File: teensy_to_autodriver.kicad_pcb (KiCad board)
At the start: 2 copper layers, 114.3 x 50.8 mm, 11 parts, among them J1 PIN_ARRAY_5X2, J2 PIN_ARRAY_3X2, J3 PIN_ARRAY_2X1, J4 PIN_ARRAY_2X1, J5 PIN_ARRAY_2X1, J6 PIN_ARRAY_2X1, M0 VAL**, M1 VAL**, M2 VAL**, M3 VAL**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

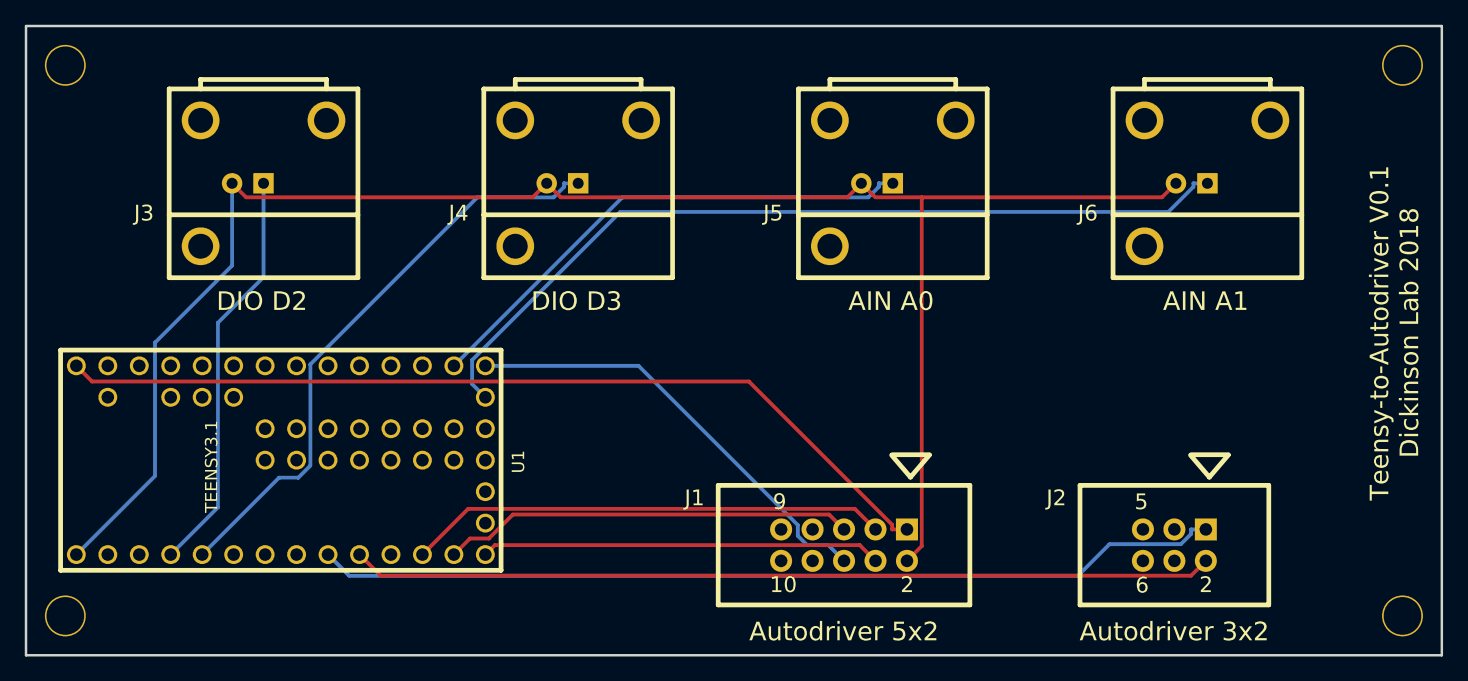
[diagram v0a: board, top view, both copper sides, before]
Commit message: Created version 0.2 of design. Added header for angle sensor.
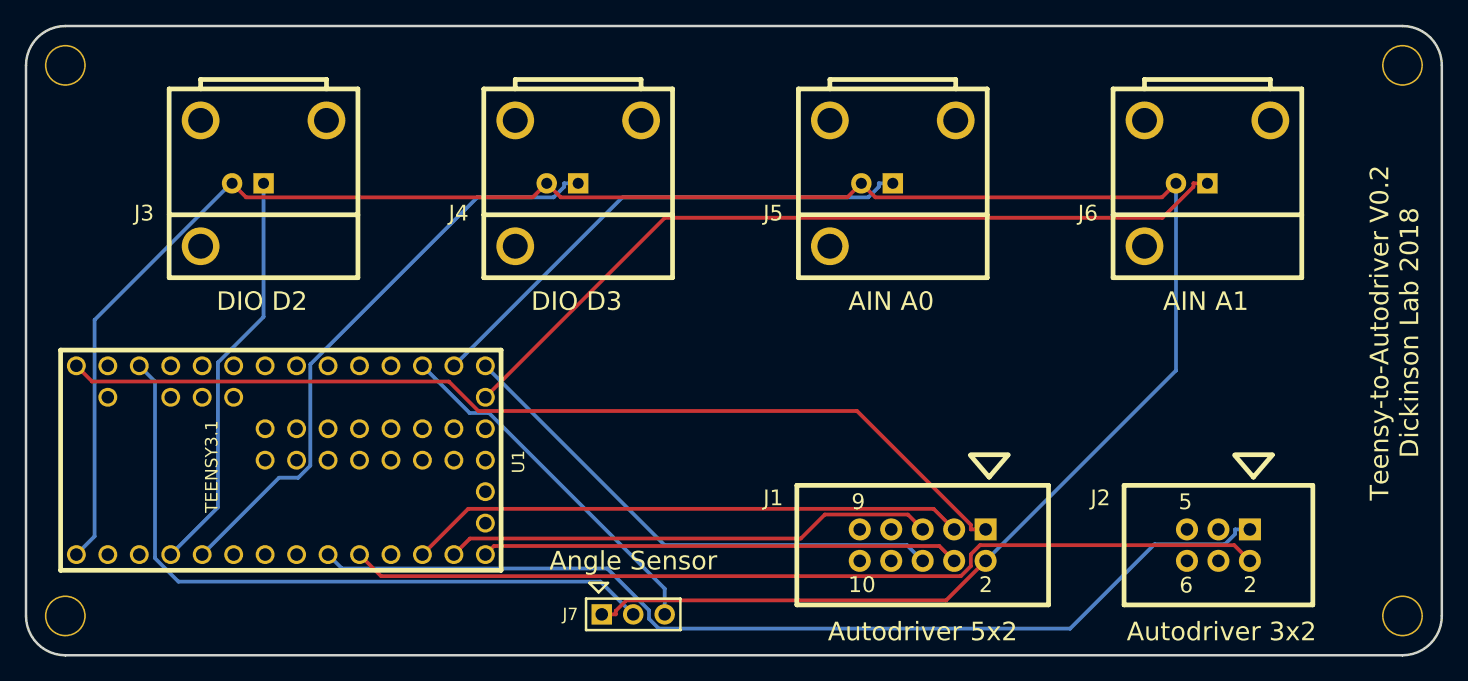
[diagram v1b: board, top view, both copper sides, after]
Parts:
- added J7: PIN_ARRAY_3X1, HEADER_3X1:HEADER_3X1, F.Cu at (99.8, 98.3)
- moved J1 6.35 mm to (123.2, 92.7)
- moved J2 3.56 mm to (147.1, 92.7)
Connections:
- U1 pad 22: Net-(U1-Pad22) -> /A1
- U1 pad 31: Net-(U1-Pad31) -> /3V3
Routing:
- net /3V3: track 0.00 -> 56.5 mm
- net GND: track 144.0 -> 184.0 mm
- net /A1: track 0.00 -> 29.1 mm
- net /~RESET: track 73.3 -> 80.8 mm
- net /~CS: track 38.8 -> 45.1 mm
- net /MOSI: track 33.3 -> 39.7 mm
- net /+5V: track 72.7 -> 79.1 mm
- net /MISO: track 32.3 -> 38.6 mm
- net /SCK: track 36.0 -> 41.8 mm
- net /~BUSY: track 69.5 -> 74.7 mm
- net /DAC: track 68.9 -> 65.6 mm
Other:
- outline, holes or cut-outs redrawn
- board text added: "Angle Sensor"
- board text added: "Teensy-to-Autodriver V0.2 Dickinson Lab 2018"
- board text removed: "Teensy-to-Autodriver V0.1 Dickinson Lab 2018"
